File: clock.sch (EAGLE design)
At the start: 37 parts, among them IC3 7805TV, J1 J10MM, J2 J10MM, J3 J7MM, J4 J7MM, J5 J5MM, J6 J30MM, Q1 BC547, Q2 BC547, U1 ATTINY45-P

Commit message: change powerjack to horizontal, fix DRC errors, mirror logos and text, add gnd plane, set wire width to 12mil
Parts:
- POWER_JACK: value KLDVX-0202-B -> DCJ0202; device con-kycon:KLDVX-0202-B -> con-jack:DCJ0202
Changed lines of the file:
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@@
 <part name="SV1" library="con-harting-ml" deviceset="ML10" device=""/>
 <part name="POWER_CLAMP" library="con-wago-508" deviceset="W237-02P" device=""/>
-<part name="POWER_JACK" library="con-kycon" deviceset="KLDVX-0202-" device="B"/>
+<part name="POWER_JACK" library="con-jack" deviceset="DCJ0202" device=""/>
 <part name="Q1" library="transistor-npn" deviceset="BC547*" device=""/>
 <part name="Q2" library="transistor-npn" deviceset="BC547*" device=""/>
@@
 <instance part="POWER_CLAMP" gate="-1" x="-58.42" y="134.62"/>
 <instance part="POWER_CLAMP" gate="-2" x="-58.42" y="129.54"/>
-<instance part="POWER_JACK" gate="G$1" x="-60.96" y="144.78" rot="MR0"/>
+<instance part="POWER_JACK" gate="G$1" x="-60.96" y="144.78"/>
 <instance part="Q1" gate="G$1" x="-38.1" y="53.34"/>
 <instance part="Q2" gate="G$1" x="-27.94" y="40.64" rot="R180"/>
@@
 <wire x1="-45.72" y1="129.54" x2="-45.72" y2="142.24" width="0.1524" layer="91"/>
 <pinref part="POWER_JACK" gate="G$1" pin="2"/>
-<wire x1="-45.72" y1="142.24" x2="-53.34" y2="142.24" width="0.1524" layer="91"/>
+<wire x1="-45.72" y1="142.24" x2="-45.72" y2="144.78" width="0.1524" layer="91"/>
+<wire x1="-45.72" y1="144.78" x2="-53.34" y2="144.78" width="0.1524" layer="91"/>
 <junction x="-45.72" y="129.54"/>
-<pinref part="POWER_JACK" gate="G$1" pin="3"/>
-<wire x1="-53.34" y1="144.78" x2="-45.72" y2="144.78" width="0.1524" layer="91"/>
-<wire x1="-45.72" y1="144.78" x2="-45.72" y2="142.24" width="0.1524" layer="91"/>
-<junction x="-45.72" y="142.24"/>
 <pinref part="C1" gate="G$1" pin="2"/>
 <wire x1="-33.02" y1="134.62" x2="-33.02" y2="129.54" width="0.1524" layer="91"/>
@@
 <junction x="-33.02" y="129.54"/>
 <pinref part="J4" gate="1" pin="1"/>
+<pinref part="POWER_JACK" gate="G$1" pin="3"/>
+<wire x1="-53.34" y1="142.24" x2="-45.72" y2="142.24" width="0.1524" layer="91"/>
+<junction x="-45.72" y="142.24"/>
 </segment>
 <segment>

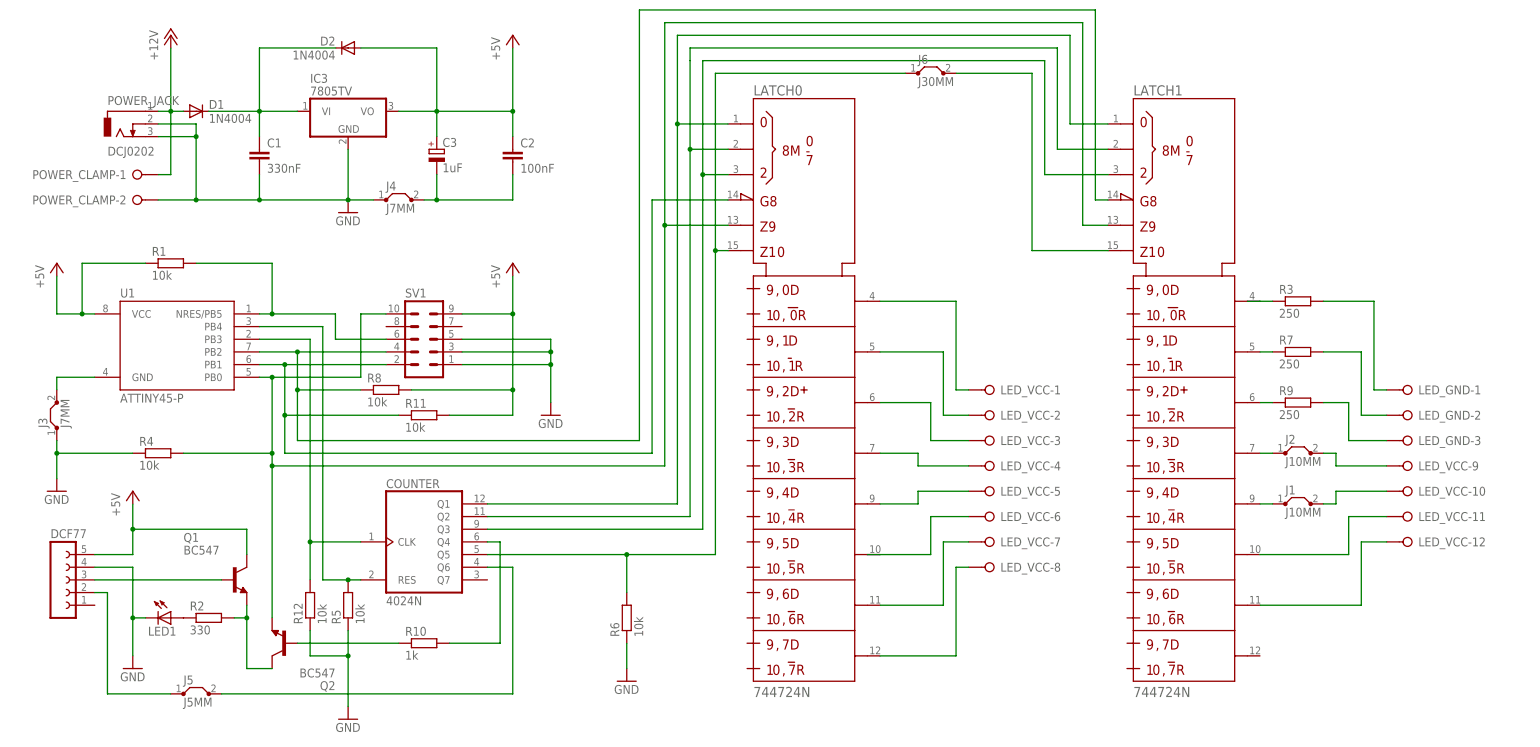
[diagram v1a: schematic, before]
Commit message: fix ERC errors of schematic, add missing VCC/VSS pins of ICs, replace jumpers with vias
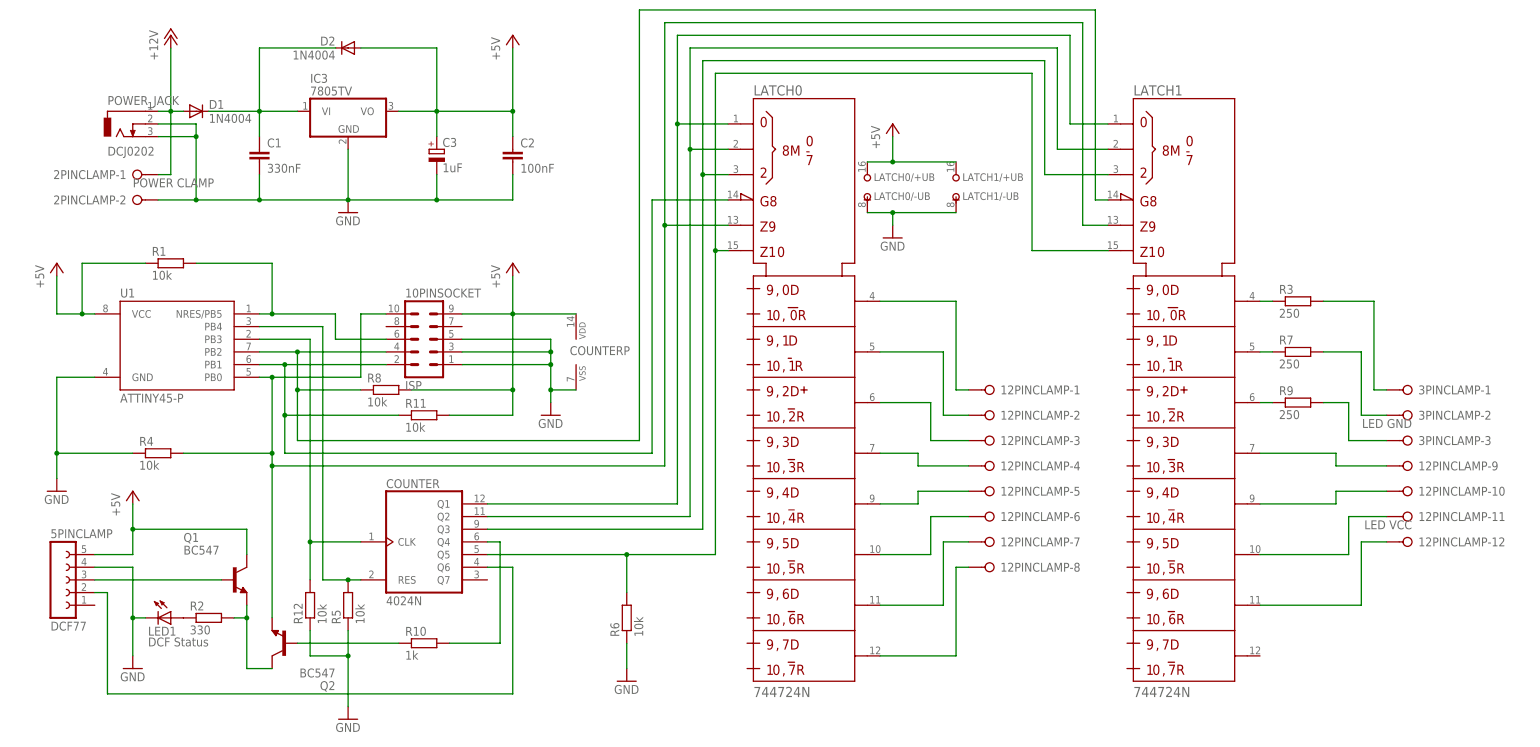
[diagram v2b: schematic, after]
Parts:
- removed J1, J2: J10MM, jumper:J10MM
- removed J3, J4: J7MM, jumper:J7MM
- removed J5: J5MM, jumper:J5MM
- removed J6: J30MM, jumper:J30MM
- 10PINSOCKET: value (none) -> ISP
- 12PINCLAMP: value (none) -> LED VCC
- 2PINCLAMP: value (none) -> POWER CLAMP
- 3PINCLAMP: value (none) -> LED GND
- 5PINCLAMP: value (none) -> DCF77
- LED1: value (none) -> DCF Status
- renumbered DCF77 to 5PINCLAMP, LED_GND to 3PINCLAMP, LED_VCC to 12PINCLAMP, POWER_CLAMP to 2PINCLAMP, SV1 to 10PINSOCKET
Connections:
- removed net N$12: 12PINCLAMP-10.KL, J1.2
- removed net N$29: LATCH11.S1
- removed net N$31: J2.1, LATCH11.Q3
- removed net N$32: 5PINCLAMP.2, J5.1
- removed net N$33: J6.2, LATCH11.CLR
- net +5V: now also COUNTERP.VDD, LATCH0/+UB.+UB, LATCH1/+UB.+UB
- net DCF_PON: now also 5PINCLAMP.2; no longer J5.2
- net GND: now also COUNTERP.VSS, LATCH0/-UB.-UB, LATCH1/-UB.-UB; no longer J3.1, J3.2, J4.1, J4.2
- net N$11: now also LATCH11.Q3; no longer J2.2
- net N$22: now also LATCH11.CLR; no longer J6.1
- net N$28: now also LATCH11.S1
- net N$30: now also 12PINCLAMP-10.KL; no longer J1.1

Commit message: rotate isp 180°, connect 4th gnd pin, move logo/text to doc layer
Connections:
- net +5V: now also 10PINSOCKET.2; no longer 10PINSOCKET.9
- net DATA: now also 10PINSOCKET.1; no longer 10PINSOCKET.10
- net GND: now also 10PINSOCKET.10, 10PINSOCKET.4, 10PINSOCKET.6, 10PINSOCKET.8; no longer 10PINSOCKET.1, 10PINSOCKET.3, 10PINSOCKET.5
- net LATCH0: now also 10PINSOCKET.7; no longer 10PINSOCKET.4
- net LATCH1: now also 10PINSOCKET.9; no longer 10PINSOCKET.2
- net N$23: now also 10PINSOCKET.5; no longer 10PINSOCKET.6
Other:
- moved on the sheet: 10PINSOCKET
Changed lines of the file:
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@@
 <instance part="D1" gate="1" x="-45.72" y="147.32"/>
 <instance part="LED1" gate="G$1" x="-50.8" y="45.72" rot="R270"/>
-<instance part="10PINSOCKET" gate="G$1" x="0" y="101.6"/>
+<instance part="10PINSOCKET" gate="G$1" x="0" y="101.6" rot="R180"/>
 <instance part="2PINCLAMP" gate="-1" x="-58.42" y="134.62"/>
 <instance part="2PINCLAMP" gate="-2" x="-58.42" y="129.54"/>
@@
 </segment>
 <segment>
-<pinref part="10PINSOCKET" gate="G$1" pin="5"/>
 <pinref part="GND2" gate="1" pin="GND"/>
 <wire x1="7.62" y1="101.6" x2="25.4" y2="101.6" width="0.1524" layer="91"/>
 <wire x1="25.4" y1="101.6" x2="25.4" y2="99.06" width="0.1524" layer="91"/>
-<pinref part="10PINSOCKET" gate="G$1" pin="1"/>
 <wire x1="25.4" y1="99.06" x2="25.4" y2="96.52" width="0.1524" layer="91"/>
 <wire x1="25.4" y1="96.52" x2="25.4" y2="91.44" width="0.1524" layer="91"/>
 <wire x1="25.4" y1="91.44" x2="25.4" y2="88.9" width="0.1524" layer="91"/>
 <wire x1="7.62" y1="96.52" x2="25.4" y2="96.52" width="0.1524" layer="91"/>
-<pinref part="10PINSOCKET" gate="G$1" pin="3"/>
-<wire x1="7.62" y1="99.06" x2="25.4" y2="99.06" width="0.1524" layer="91"/>
 <junction x="25.4" y="96.52"/>
 <junction x="25.4" y="99.06"/>
 <pinref part="COUNTER" gate="P" pin="VSS"/>
+<wire x1="7.62" y1="99.06" x2="25.4" y2="99.06" width="0.1524" layer="91"/>
 <wire x1="30.48" y1="91.44" x2="25.4" y2="91.44" width="0.1524" layer="91"/>
 <junction x="25.4" y="91.44"/>
+<pinref part="10PINSOCKET" gate="G$1" pin="10"/>
+<pinref part="10PINSOCKET" gate="G$1" pin="8"/>
+<pinref part="10PINSOCKET" gate="G$1" pin="6"/>
+<pinref part="10PINSOCKET" gate="G$1" pin="4"/>
+<wire x1="7.62" y1="104.14" x2="25.4" y2="104.14" width="0.1524" layer="91"/>
+<wire x1="25.4" y1="104.14" x2="25.4" y2="101.6" width="0.1524" layer="91"/>
+<junction x="25.4" y="101.6"/>
 </segment>
 <segment>
@@
 </segment>
 <segment>
-<pinref part="10PINSOCKET" gate="G$1" pin="9"/>
 <pinref part="P+3" gate="1" pin="+5V"/>
 <wire x1="7.62" y1="106.68" x2="17.78" y2="106.68" width="0.1524" layer="91"/>
@@
 <pinref part="COUNTER" gate="P" pin="VDD"/>
 <wire x1="30.48" y1="106.68" x2="17.78" y2="106.68" width="0.1524" layer="91"/>
+<pinref part="10PINSOCKET" gate="G$1" pin="2"/>
 </segment>
 <segment>
@@
 <pinref part="Q2" gate="G$1" pin="E"/>
 <pinref part="U1" gate="G$1" pin="PB0"/>
-<pinref part="10PINSOCKET" gate="G$1" pin="10"/>
-<wire x1="-7.62" y1="106.68" x2="-12.7" y2="106.68" width="0.1524" layer="91"/>
 <wire x1="-12.7" y1="106.68" x2="-12.7" y2="93.98" width="0.1524" layer="91"/>
 <wire x1="-12.7" y1="93.98" x2="-30.48" y2="93.98" width="0.1524" layer="91"/>
@@
 <pinref part="LATCH1" gate="1" pin="D"/>
 <wire x1="132.08" y1="124.46" x2="137.16" y2="124.46" width="0.1524" layer="91"/>
+<pinref part="10PINSOCKET" gate="G$1" pin="1"/>
+<wire x1="-12.7" y1="106.68" x2="-7.62" y2="106.68" width="0.1524" layer="91"/>
 </segment>
 </net>
 <net name="LATCH0" class="0">
 <segment>
-<pinref part="10PINSOCKET" gate="G$1" pin="4"/>
 <pinref part="U1" gate="G$1" pin="PB2"/>
 <wire x1="-7.62" y1="99.06" x2="-25.4" y2="99.06" width="0.1524" layer="91"/>
@@
 <wire x1="-12.7" y1="91.44" x2="-25.4" y2="91.44" width="0.1524" layer="91"/>
 <junction x="-25.4" y="91.44"/>
+<pinref part="10PINSOCKET" gate="G$1" pin="7"/>
 </segment>
 </net>
 <net name="LATCH1" class="0">
 <segment>
-<pinref part="10PINSOCKET" gate="G$1" pin="2"/>
 <pinref part="U1" gate="G$1" pin="PB1"/>
 <wire x1="-7.62" y1="96.52" x2="-27.94" y2="96.52" width="0.1524" layer="91"/>
@@
 <wire x1="-5.08" y1="86.36" x2="-27.94" y2="86.36" width="0.1524" layer="91"/>
 <junction x="-27.94" y="86.36"/>
+<pinref part="10PINSOCKET" gate="G$1" pin="9"/>
 </segment>
 </net>
@@
 <wire x1="-45.72" y1="116.84" x2="-30.48" y2="116.84" width="0.1524" layer="91"/>
 <pinref part="U1" gate="G$1" pin="NRES/PB5"/>
-<pinref part="10PINSOCKET" gate="G$1" pin="6"/>
 <wire x1="-7.62" y1="101.6" x2="-17.78" y2="101.6" width="0.1524" layer="91"/>
 <wire x1="-17.78" y1="101.6" x2="-17.78" y2="106.68" width="0.1524" layer="91"/>
@@
 <wire x1="-30.48" y1="116.84" x2="-30.48" y2="106.68" width="0.1524" layer="91"/>
 <junction x="-30.48" y="106.68"/>
-</segment>
-</net>
+<pinref part="10PINSOCKET" gate="G$1" pin="5"/>
+</segment>
+</net>
